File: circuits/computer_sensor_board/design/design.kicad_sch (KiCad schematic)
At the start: 1 part, among them U1 TDN_5-2411WISM

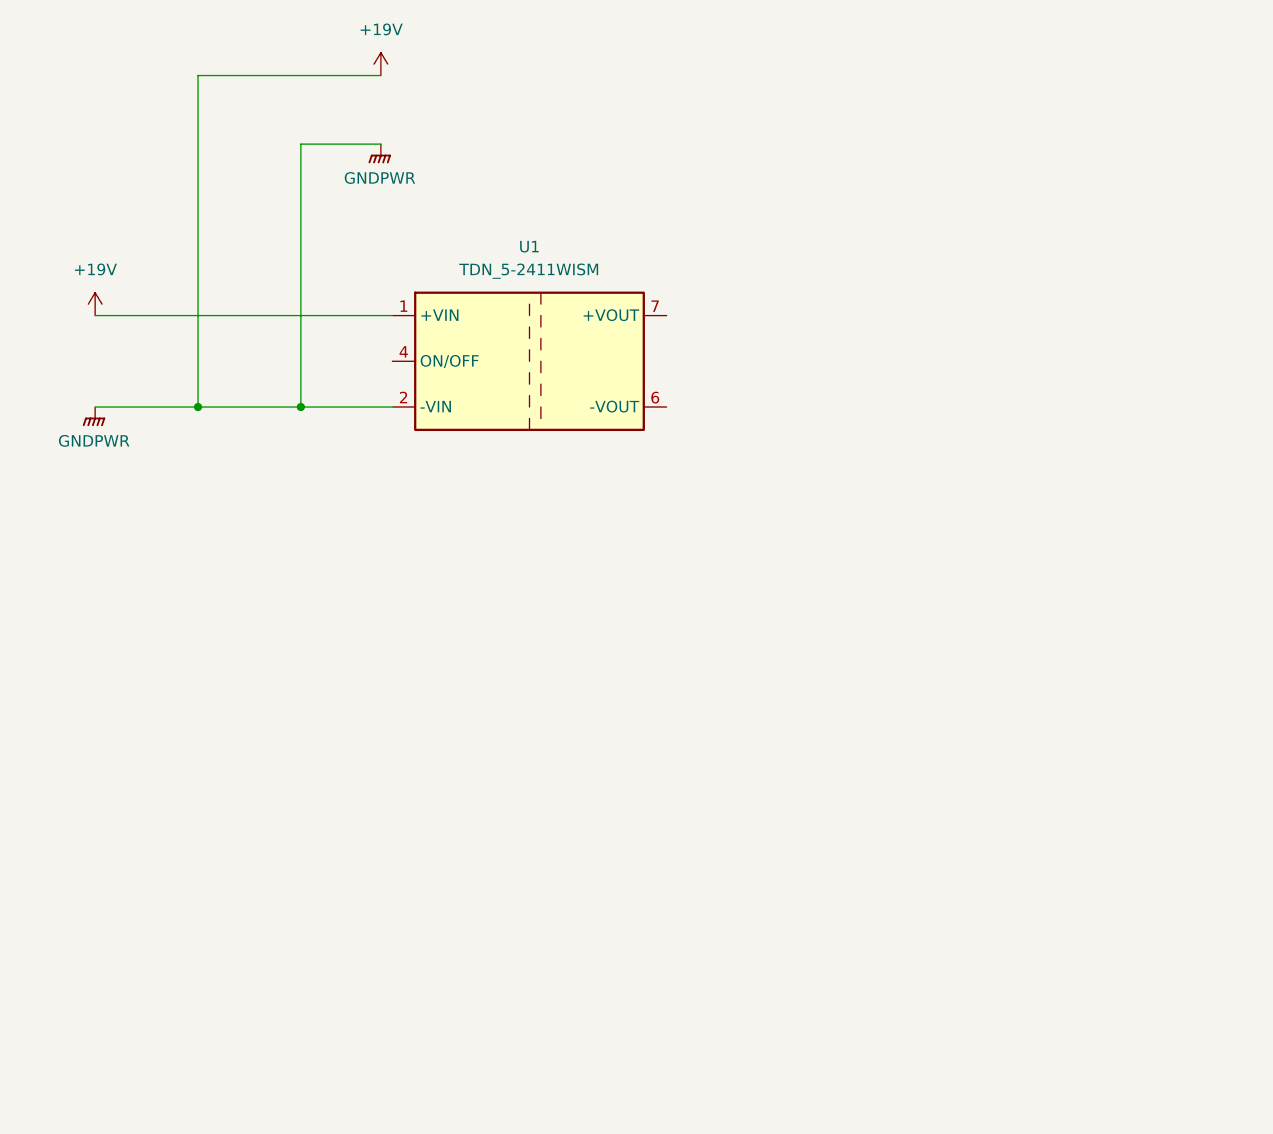
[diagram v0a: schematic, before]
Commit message: add teensy
Signed-off-by: Masaya Kataoka <ms.kataoka@gmail.com>
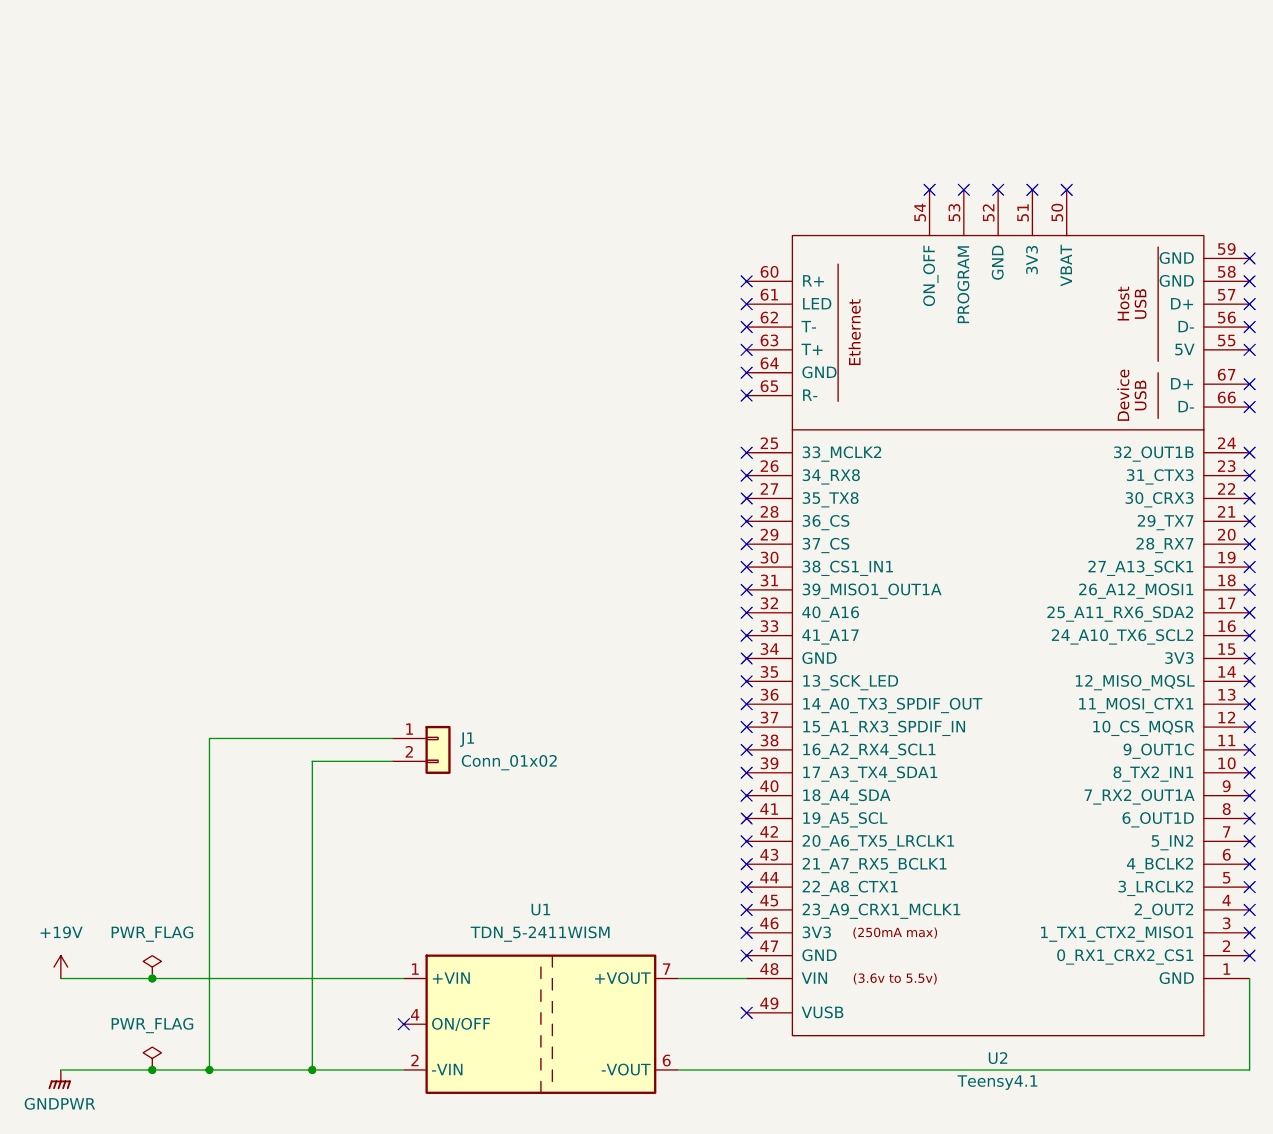
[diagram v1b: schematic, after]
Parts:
- added J1: Conn_01x02, symbol Connector_Generic:Conn_01x02
- added U2: Teensy4.1, symbol teensy:Teensy4.1
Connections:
- net +19V: no longer U1.2 (-VIN)
- net at U1.6 (-VOUT): now also U2.1 (GND)
- net at U1.7 (+VOUT): now also U2.48 (VIN)
- new net GNDPWR: J1.1 (Pin_1), J1.2 (Pin_2), U1.2 (-VIN)
- no-connect marks 0 -> 66
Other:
- moved on the sheet: U1
